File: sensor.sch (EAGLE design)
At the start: 17 parts, among them IC1 TINY261A

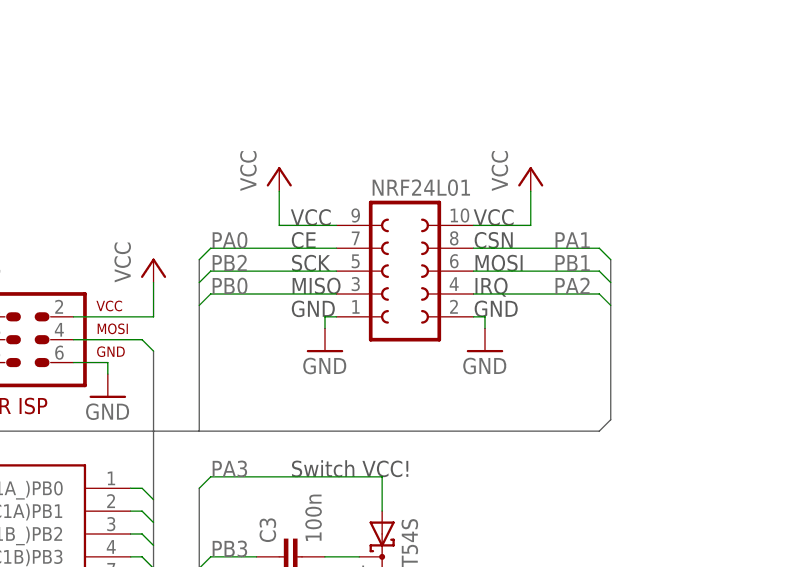
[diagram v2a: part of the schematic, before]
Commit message: series resistors for shared spi/isp interface
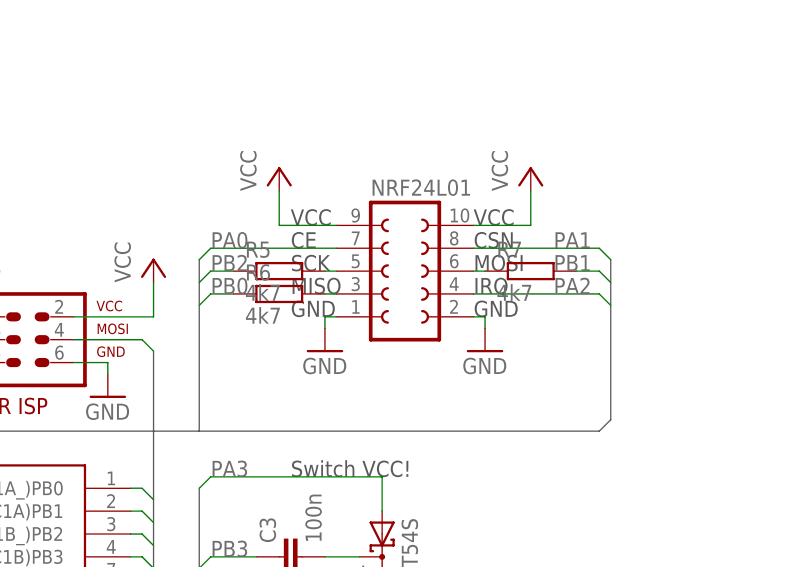
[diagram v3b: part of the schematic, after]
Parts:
- added R5, R6, R7: 4k7, rcl:R-EU_0207/7
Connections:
- new net N$3: NRF24L01.5, R5.2
- new net N$4: NRF24L01.3, R6.2
- new net N$5: NRF24L01.6, R7.1
- net PB0: now also R6.1; no longer NRF24L01.3
- net PB1: now also R7.2; no longer NRF24L01.6
- net PB2: now also R5.1; no longer NRF24L01.5
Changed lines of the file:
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@@
 <part name="GND8" library="supply1" deviceset="GND" device=""/>
 <part name="FRAME2" library="frames" deviceset="DINA5_P" device=""/>
+<part name="R5" library="rcl" deviceset="R-EU_" device="0207/7" value="4k7"/>
+<part name="R6" library="rcl" deviceset="R-EU_" device="0207/7" value="4k7"/>
+<part name="R7" library="rcl" deviceset="R-EU_" device="0207/7" value="4k7"/>
 </parts>
 <sheets>
@@
 <instance part="GND8" gate="1" x="31.75" y="46.99"/>
 <instance part="FRAME2" gate="G$1" x="0" y="0"/>
+<instance part="R5" gate="G$1" x="81.28" y="140.97"/>
+<instance part="R6" gate="G$1" x="81.28" y="138.43"/>
+<instance part="R7" gate="G$1" x="109.22" y="140.97"/>
 </instances>
 <busses>
@@
 </segment>
 <segment>
-<pinref part="NRF24L01" gate="G$1" pin="3"/>
-<wire x1="87.63" y1="138.43" x2="73.66" y2="138.43" width="0.1524" layer="91"/>
 <label x="73.66" y="138.43" size="1.778" layer="95"/>
 <wire x1="72.39" y1="137.16" x2="73.66" y2="138.43" width="0.1524" layer="91"/>
+<pinref part="R6" gate="G$1" pin="1"/>
+<wire x1="73.66" y1="138.43" x2="76.2" y2="138.43" width="0.1524" layer="91"/>
 </segment>
 </net>
@@
 </segment>
 <segment>
-<pinref part="NRF24L01" gate="G$1" pin="6"/>
-<wire x1="116.84" y1="140.97" x2="102.87" y2="140.97" width="0.1524" layer="91"/>
 <label x="111.76" y="140.97" size="1.778" layer="95"/>
 <wire x1="118.11" y1="139.7" x2="116.84" y2="140.97" width="0.1524" layer="91"/>
+<pinref part="R7" gate="G$1" pin="2"/>
+<wire x1="116.84" y1="140.97" x2="114.3" y2="140.97" width="0.1524" layer="91"/>
 </segment>
 </net>
 <net name="PB2" class="0">
 <segment>
-<pinref part="NRF24L01" gate="G$1" pin="5"/>
-<wire x1="73.66" y1="140.97" x2="87.63" y2="140.97" width="0.1524" layer="91"/>
 <wire x1="73.66" y1="140.97" x2="72.39" y2="139.7" width="0.1524" layer="91"/>
 <label x="73.66" y="140.97" size="1.778" layer="95"/>
+<pinref part="R5" gate="G$1" pin="1"/>
+<wire x1="73.66" y1="140.97" x2="76.2" y2="140.97" width="0.1524" layer="91"/>
 </segment>
 <segment>
@@
 </segment>
 </net>
+<net name="N$3" class="0">
+<segment>
+<pinref part="NRF24L01" gate="G$1" pin="5"/>
+<pinref part="R5" gate="G$1" pin="2"/>
+<wire x1="87.63" y1="140.97" x2="86.36" y2="140.97" width="0.1524" layer="91"/>
+</segment>
+</net>
+<net name="N$4" class="0">
+<segment>
+<pinref part="R6" gate="G$1" pin="2"/>
+<pinref part="NRF24L01" gate="G$1" pin="3"/>
+<wire x1="86.36" y1="138.43" x2="87.63" y2="138.43" width="0.1524" layer="91"/>
+</segment>
+</net>
+<net name="N$5" class="0">
+<segment>
+<pinref part="NRF24L01" gate="G$1" pin="6"/>
+<pinref part="R7" gate="G$1" pin="1"/>
+<wire x1="102.87" y1="140.97" x2="104.14" y2="140.97" width="0.1524" layer="91"/>
+</segment>
+</net>
